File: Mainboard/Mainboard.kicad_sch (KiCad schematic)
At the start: 33 parts, among them IC1 MC7805BD2TR4G, IC2 MC7805BD2TR4G, J1 26-60-4023, J2 BHR-14-VUA, J3 26-60-4023, J4 4328, U1 ISO1541

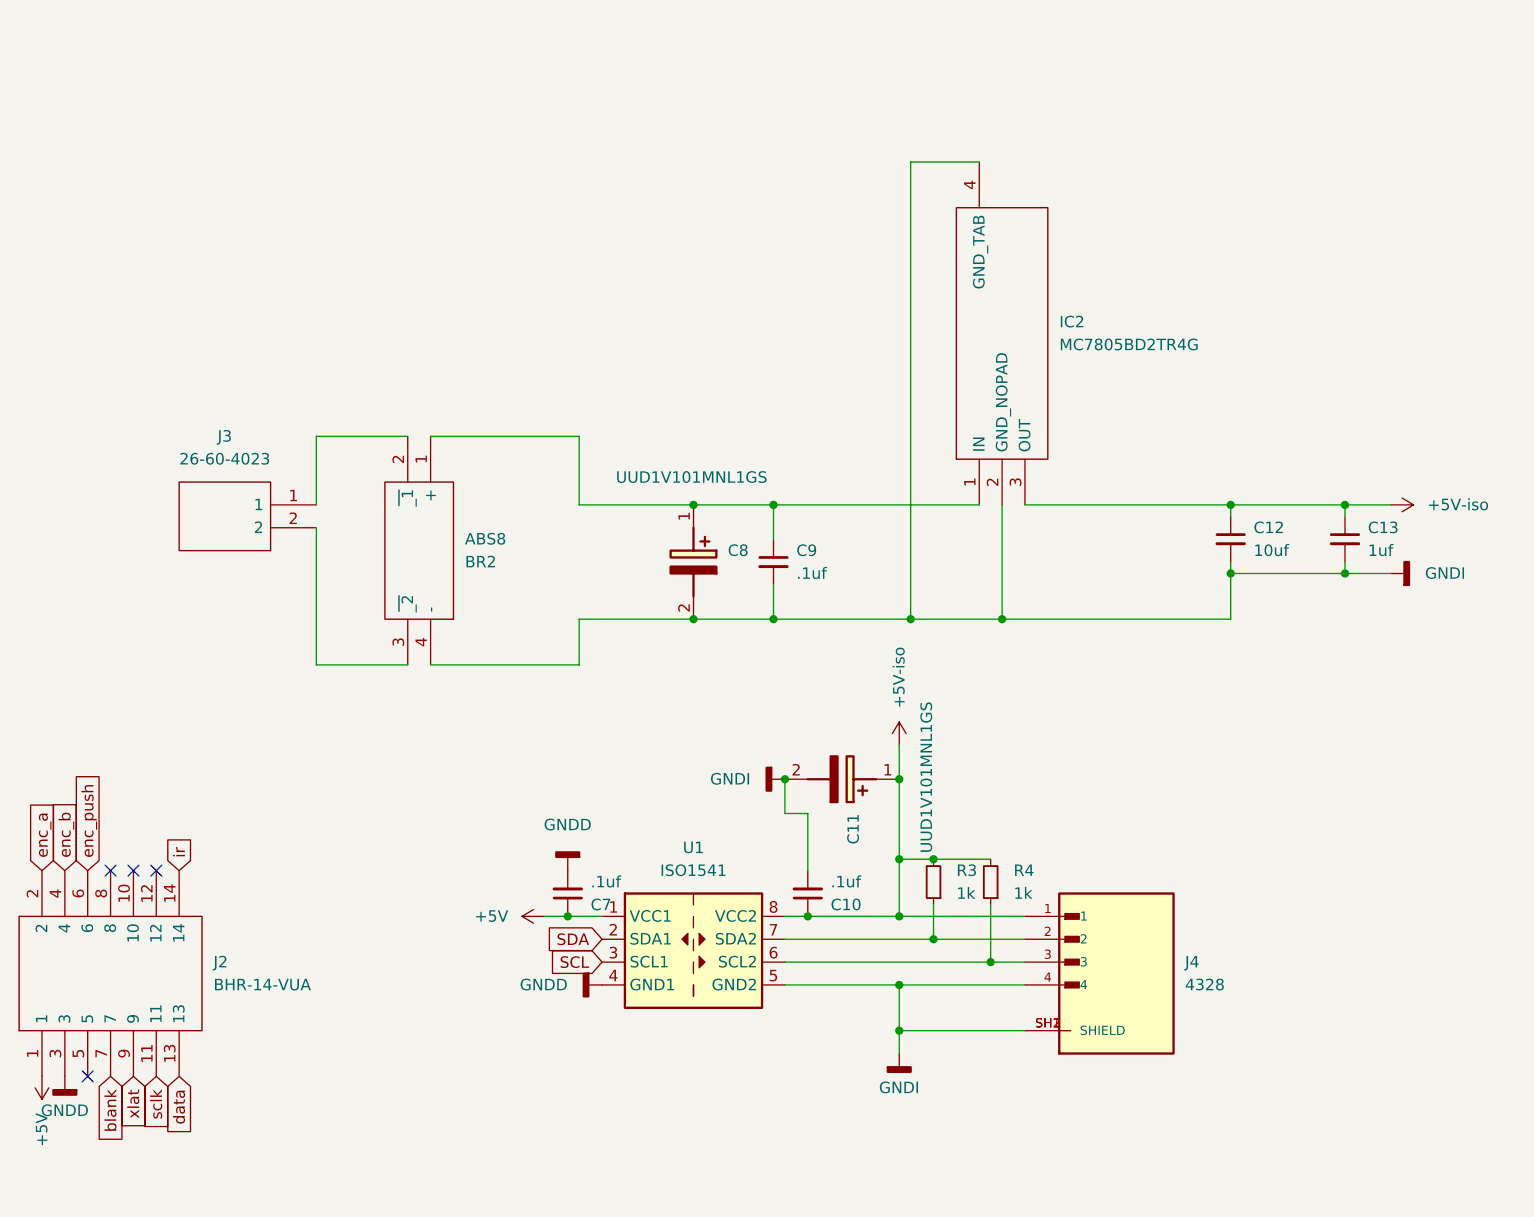
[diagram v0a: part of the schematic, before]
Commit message: moving everything onto front panel, switching psu, no iso
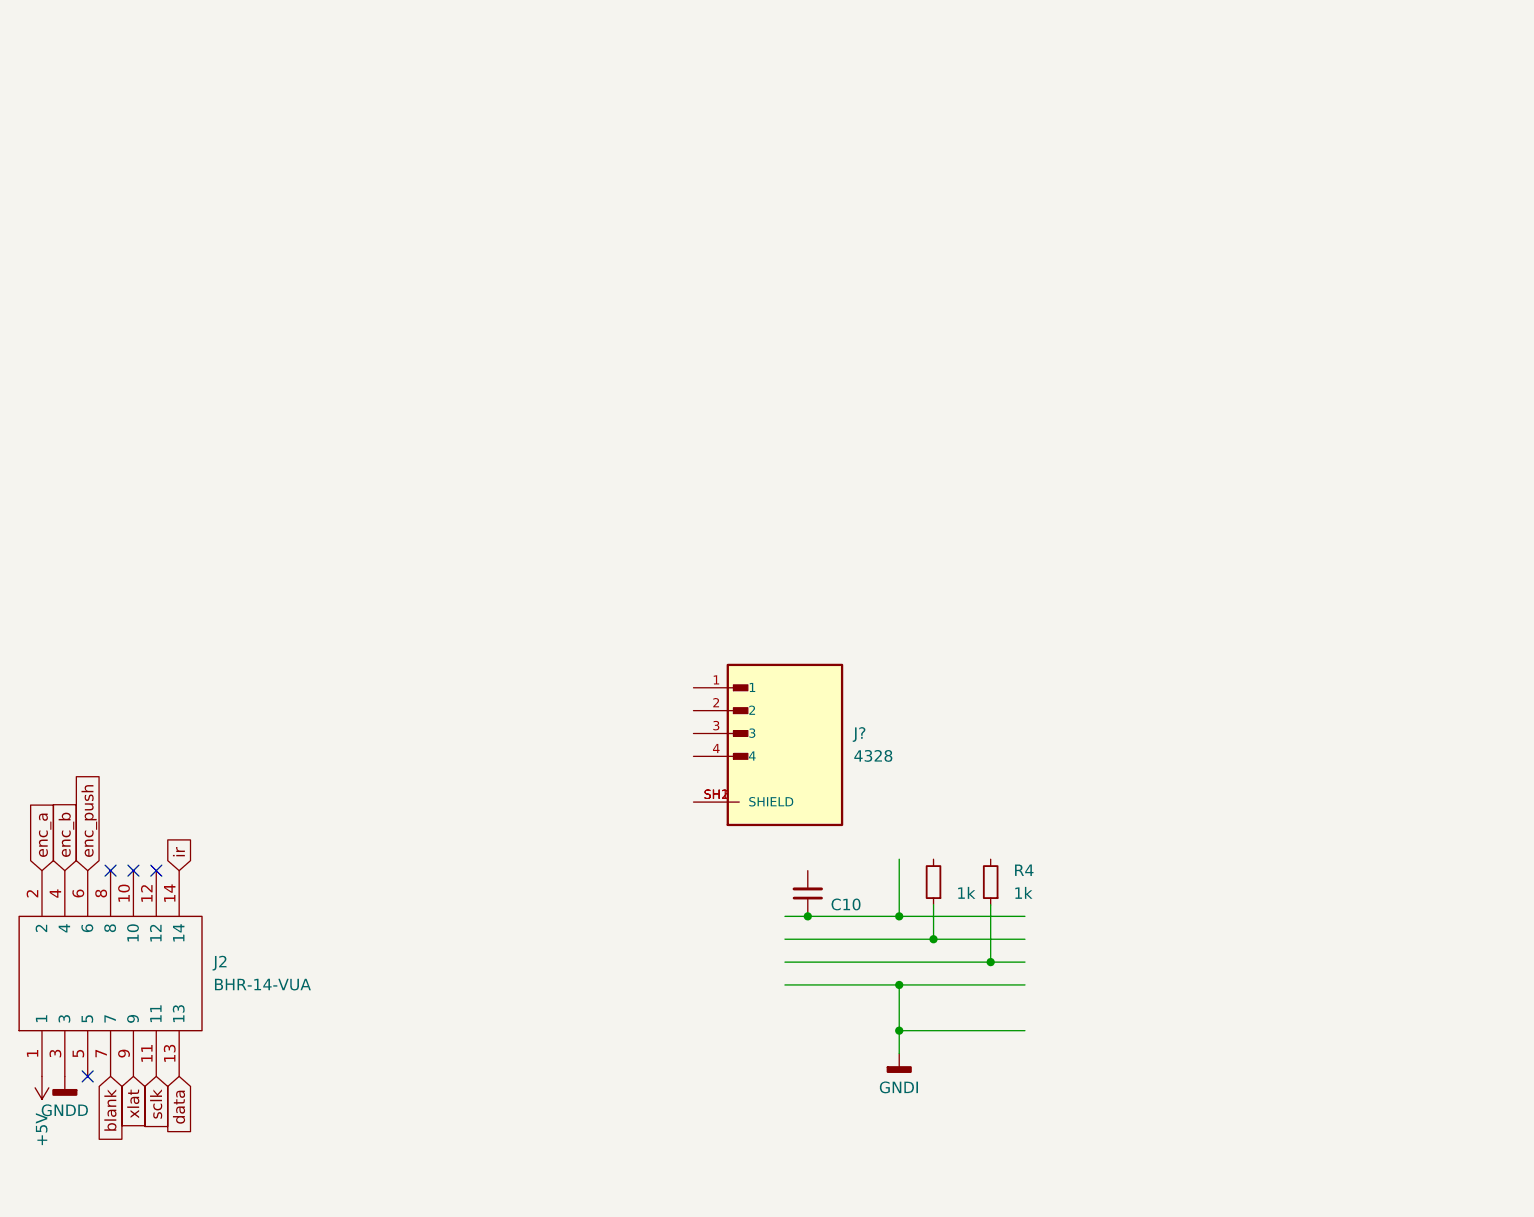
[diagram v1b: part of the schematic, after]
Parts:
- removed BR2: ABS8, Samacsys:ABS8, symbol Samacsys:ABS8
- removed C11, C8: UUD1V101MNL1GS, Samacsys:CAPAE830X1050N, symbol Samacsys_kicad_sym:UUD1V101MNL1GS
- removed C12: 10uf, Capacitor_SMD:C_1206_3216Metric, symbol Device:C_Small
- removed C13: 1uf, Capacitor_SMD:C_1206_3216Metric, symbol Device:C_Small
- removed C7, C9: .1uf, Capacitor_SMD:C_1206_3216Metric, symbol Device:C_Small
- removed IC2: MC7805BD2TR4G, Samacsys:TO254P1420X457-4N, symbol Samacsys:MC7805BD2TR4G
- removed J3: 26-60-4023, Samacsys:26604023, symbol Samacsys:26-60-4023
- removed J4: 4328, Snapeda_8:ADAFRUIT_4328, symbol Snapeda_kicad_sym:4328
- removed U1: ISO1541, Package_SO:SOIC-8_3.9x4.9mm_P1.27mm, symbol Isolator:ISO1541
- added J?: 4328, Snapeda_8:ADAFRUIT_4328, symbol Snapeda_kicad_sym:4328
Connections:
- net GNDI: no longer C10.2
- removed net +5V-iso: C10.1, R3.2, R4.2
- new net: J?.SH1 (SHIELD), J?.SH2 (SHIELD)
